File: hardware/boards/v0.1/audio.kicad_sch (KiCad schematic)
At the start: 45 parts, among them J4 SPKR_L, J5 SPKR_R, J7 HP, J8 LINE_OUT, J9 LINE_IN, U24 MIC, U28 TS5A23159RSE, U29 NAU88C22YG, U34 SI4710-B30-GMR, U35 SI4703-C19-GMR, Y3 ASVK-32.768KHZ-LJ-T

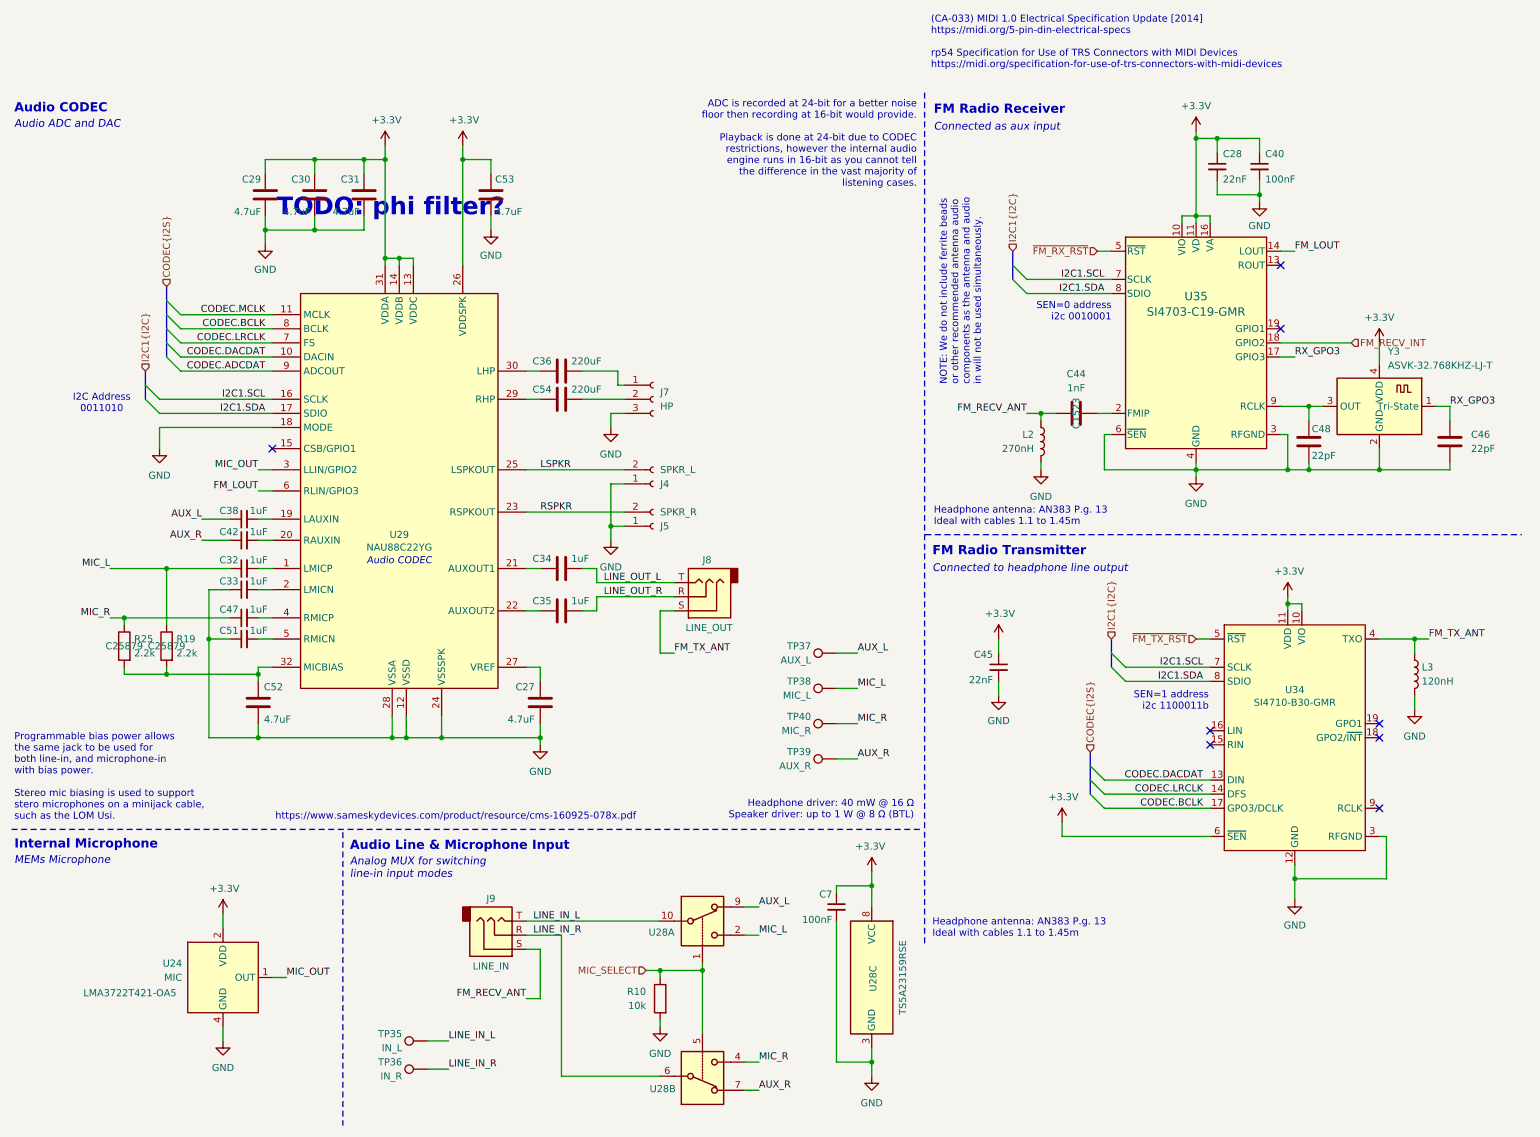
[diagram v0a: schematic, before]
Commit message: feat: various routing cleanup, add SD flash
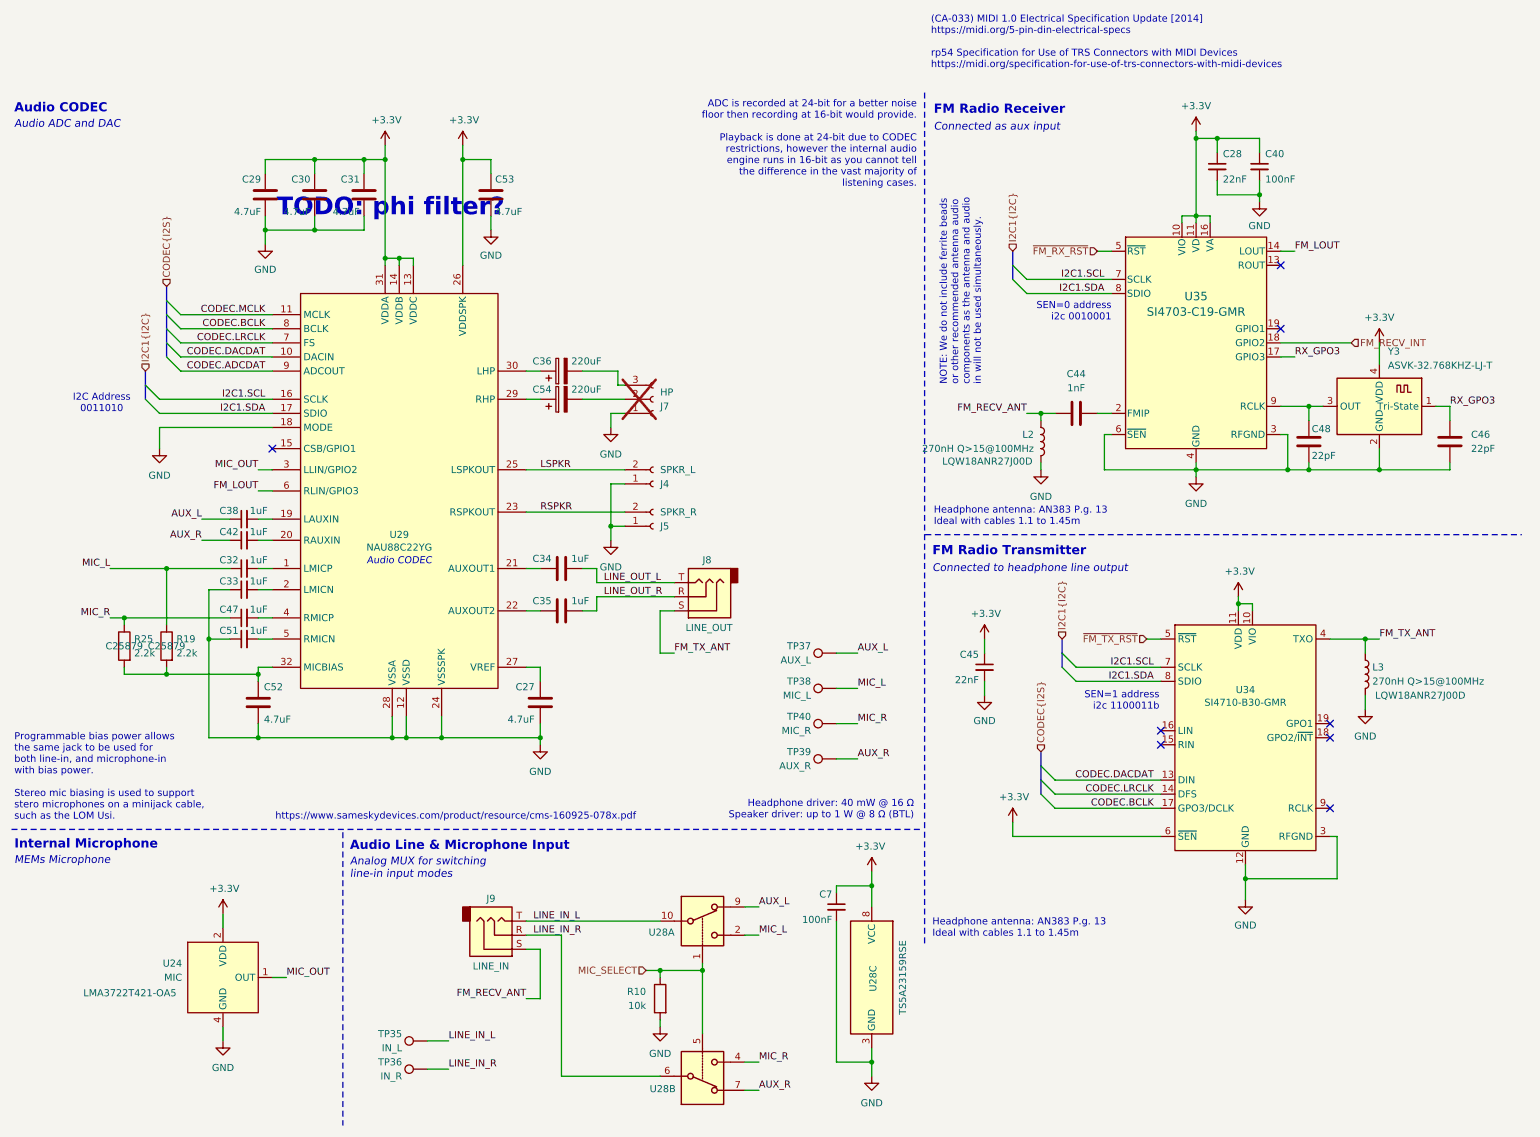
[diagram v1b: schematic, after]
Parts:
- C36: footprint Capacitor_SMD:C_0402_1005Metric -> Capacitor_SMD:CP_Elec_5x5.4; symbol Device:C -> Device:C_Polarized; JCL (none) -> C7461237
- C54: footprint Capacitor_SMD:C_0402_1005Metric -> Capacitor_SMD:CP_Elec_5x5.4; symbol Device:C -> Device:C_Polarized; JLC (none) -> C7461237
- J7: now not fitted; now left out of the parts list
- J8, J9: now left out of the parts list
- L2: value 270nH -> 270nH Q>15@100MHz; JLC (none) -> C98093; Part (none) -> LQW18ANR27J00D
- L3: value 120nH -> 270nH Q>15@100MHz; JLC (none) -> C98093; Part (none) -> LQW18ANR27J00D
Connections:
- net EPAD: now also J7.1 (Pin_1); no longer J7.3 (Pin_3)
- net at C36.2: now also J7.3 (Pin_3); no longer J7.1 (Pin_1)
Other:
- moved on the sheet: C45, L3, U34

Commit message: chore: more schematic and routing organization
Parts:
- C36: JLC (none) -> C7461237
- J4, J5: now left out of the parts list
- U34: now not fitted; now left out of the parts list
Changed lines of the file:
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@@
 		(unit 1)
 		(exclude_from_sim no)
-		(in_bom yes)
+		(in_bom no)
 		(on_board yes)
-		(dnp no)
+		(dnp yes)
 		(property "Reference" "U34"
 			(at 234.95 119.634 0)
@@
 			)
 		)
+		(property "JLC" "C7461237"
+			(at 111.76 62.23 0)
+			(effects
+				(font
+					(size 1.27 1.27)
+				)
+			)
+		)
 		(pin "2"
 		)
@@
 		(unit 1)
 		(exclude_from_sim no)
-		(in_bom yes)
+		(in_bom no)
 		(on_board yes)
 		(dnp no)
@@
 		(unit 1)
 		(exclude_from_sim no)
-		(in_bom yes)
+		(in_bom no)
 		(on_board yes)
 		(dnp no)

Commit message: feat: more BOM selection
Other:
- note removed: "(CA-033) MIDI 1.0 Electrical Specification Update [2014] https://midi.org/5-pin-din-electrical-specs rp54 Specification for Use of TRS Connectors with MIDI Devices https://midi.org/specification-for-use-of-trs-connectors-with-midi-devices"
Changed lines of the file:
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@@
-		)
-	)
-	(text "(CA-033) MIDI 1.0 Electrical Specification Update [2014]\nhttps://midi.org/5-pin-din-electrical-specs\n\nrp54 Specification for Use of TRS Connectors with MIDI Devices\nhttps://midi.org/specification-for-use-of-trs-connectors-with-midi-devices"
-		(exclude_from_sim no)
-		(at 178.308 3.048 0)
-		(effects
-			(font
-				(size 1.27 1.27)
-				(thickness 0.1588)
-				(color 132 132 132 1)
-			)
-			(justify left)
 		)
 	)

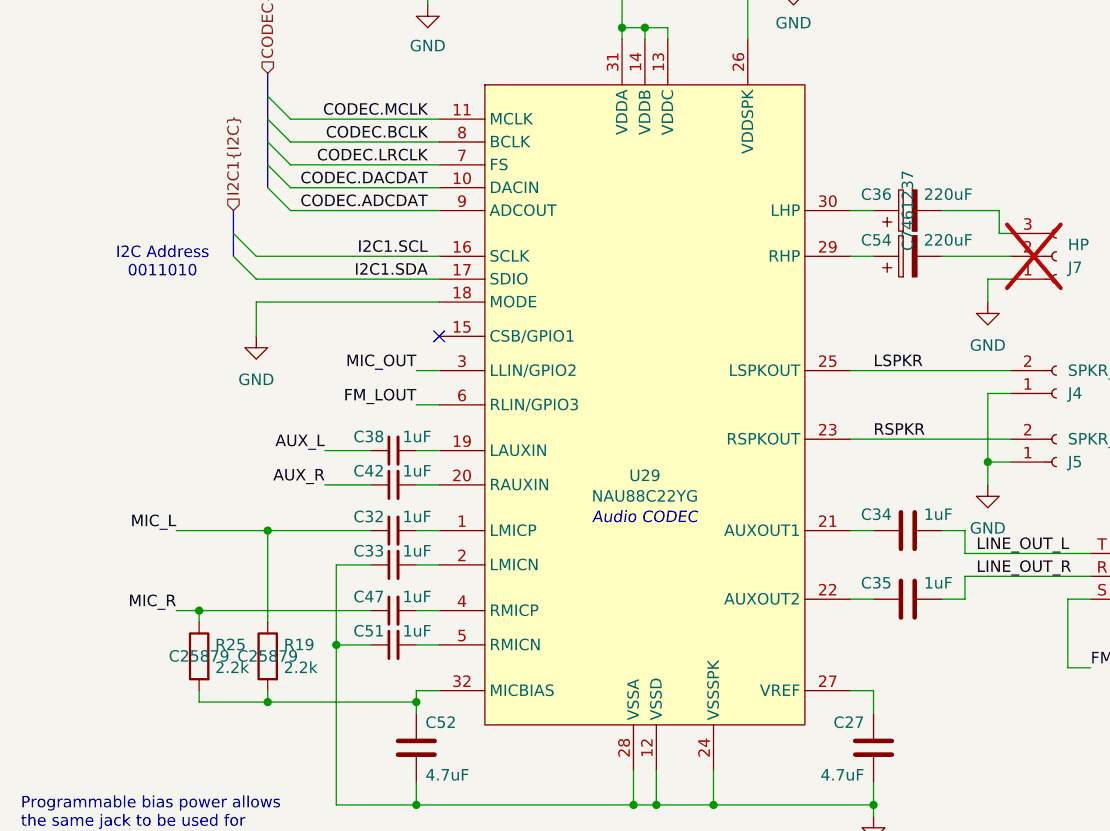
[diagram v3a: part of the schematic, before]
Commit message: feat: swap out of stock components
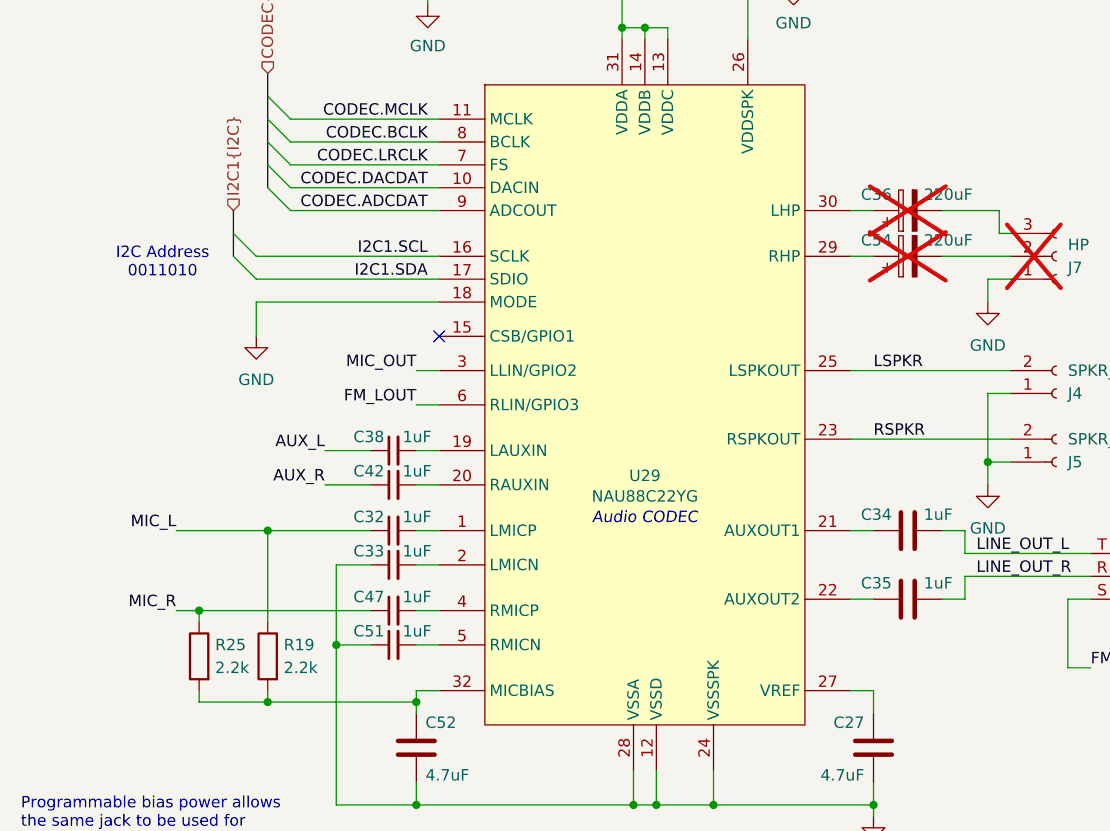
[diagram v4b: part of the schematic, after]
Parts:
- C36: JCL C7461237 -> (none); now not fitted; now left out of the parts list
- C54: now not fitted; now left out of the parts list
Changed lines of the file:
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@@
 		(unit 1)
 		(exclude_from_sim no)
-		(in_bom yes)
+		(in_bom no)
 		(on_board yes)
-		(dnp no)
+		(dnp yes)
 		(property "Reference" "C54"
 			(at 109.982 65.532 90)
@@
 					(size 1.27 1.27)
 				)
+				(hide yes)
 			)
 		)
@@
 		(unit 1)
 		(exclude_from_sim no)
-		(in_bom yes)
+		(in_bom no)
 		(on_board yes)
-		(dnp no)
+		(dnp yes)
 		(property "Reference" "C36"
 			(at 109.982 60.452 90)
@@
 			)
 		)
-		(property "JCL" "C7461237"
-			(at 111.76 62.23 90)
-			(effects
-				(font
-					(size 1.27 1.27)
-				)
-				(hide yes)
-			)
-		)
 		(property "JLC" "C7461237"
 			(at 111.76 62.23 0)
@@
 					(size 1.27 1.27)
 				)
+				(hide yes)
 			)
 		)
@@
 					(size 1.27 1.27)
 				)
+				(hide yes)
 			)
 		)

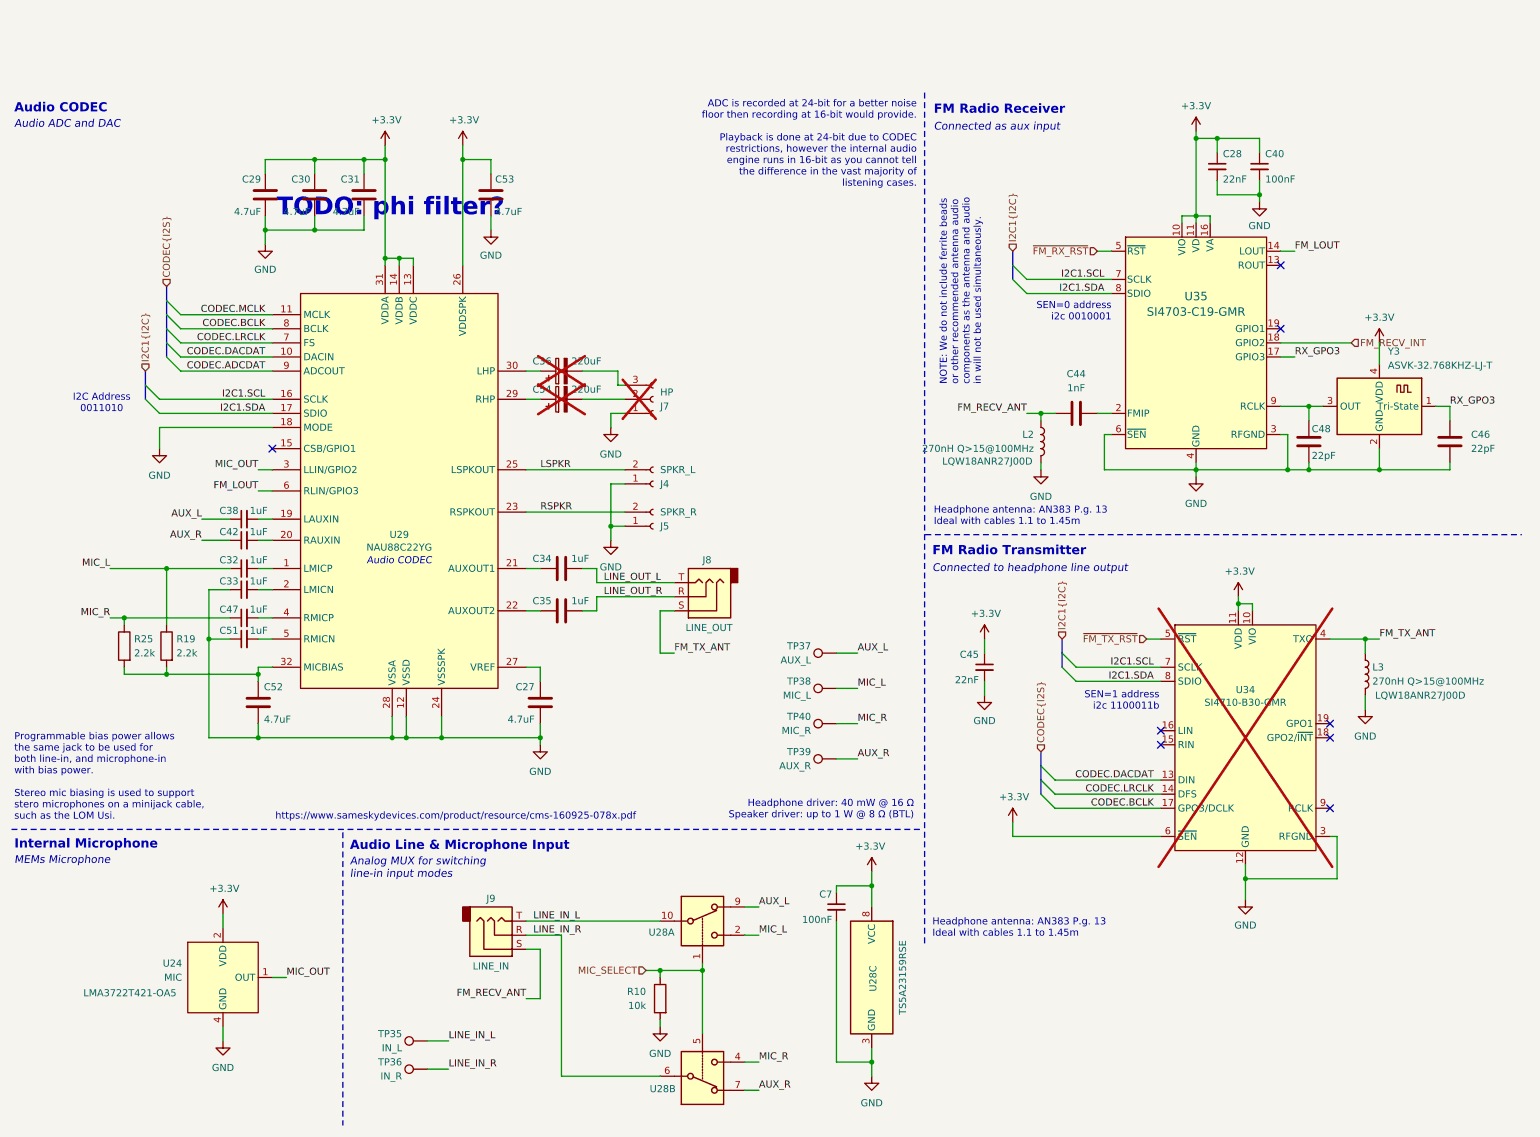
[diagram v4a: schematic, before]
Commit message: feat: various cleanup and BOM adjustment, split audio in into two switches
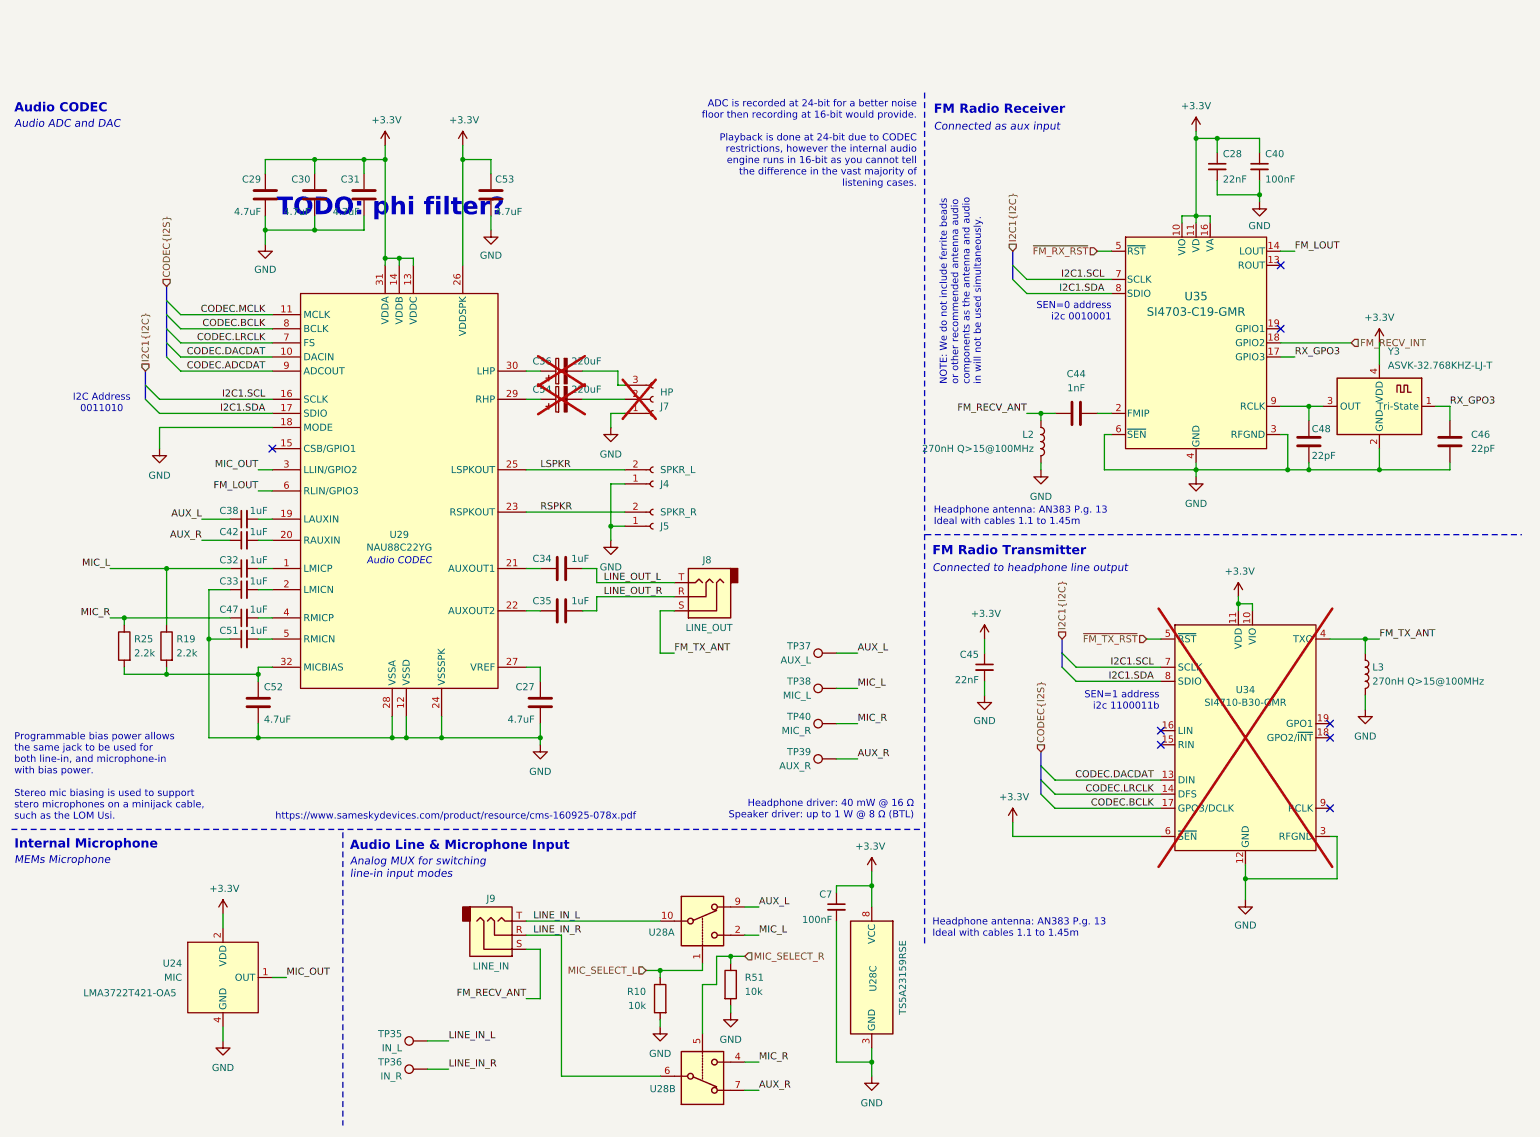
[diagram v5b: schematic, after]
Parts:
- added R51: 10k, Resistor_SMD:R_0402_1005Metric, symbol Device:R
- L2, L3: Part LQW18ANR27J00D -> (none)
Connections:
- net EPAD: now also R51.2
- net MIC_SELECT renamed MIC_SELECT_L
- net MIC_SELECT_L: no longer U28.5
- new net MIC_SELECT_R: R51.1, U28.5
